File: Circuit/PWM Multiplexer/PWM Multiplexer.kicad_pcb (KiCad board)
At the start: 2 copper layers, 63 parts, among them Q1 S8050, Q10 S8050, Q11 S8050, Q12 S8050, Q13 S8050, Q14 S8050, Q2 S8050, Q3 S8050, Q4 S8050, Q5 S8050, Q6 S8050, Q7 S8050, Q8 S8050, Q9 S8050, U1 74HC137, U2 74HC137, U3 L7805

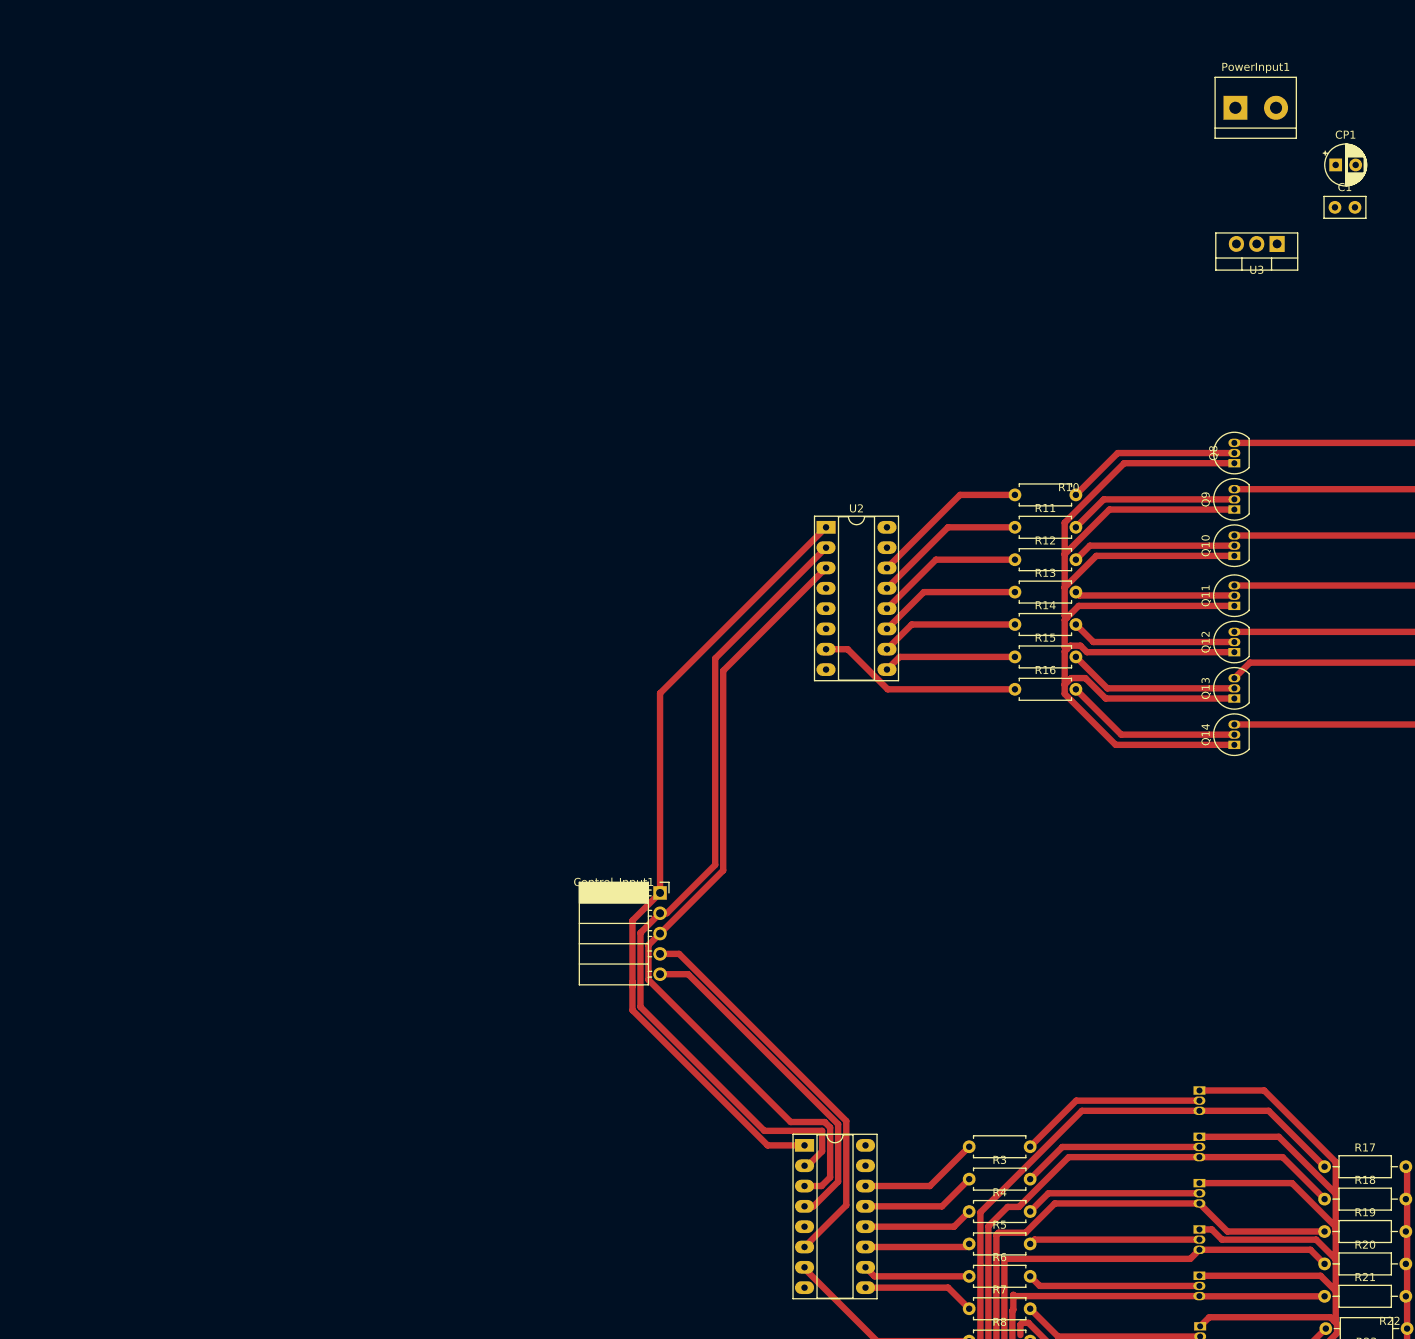
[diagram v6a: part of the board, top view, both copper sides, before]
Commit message: added optical isolation to PWM demultiplexer circuit schematic
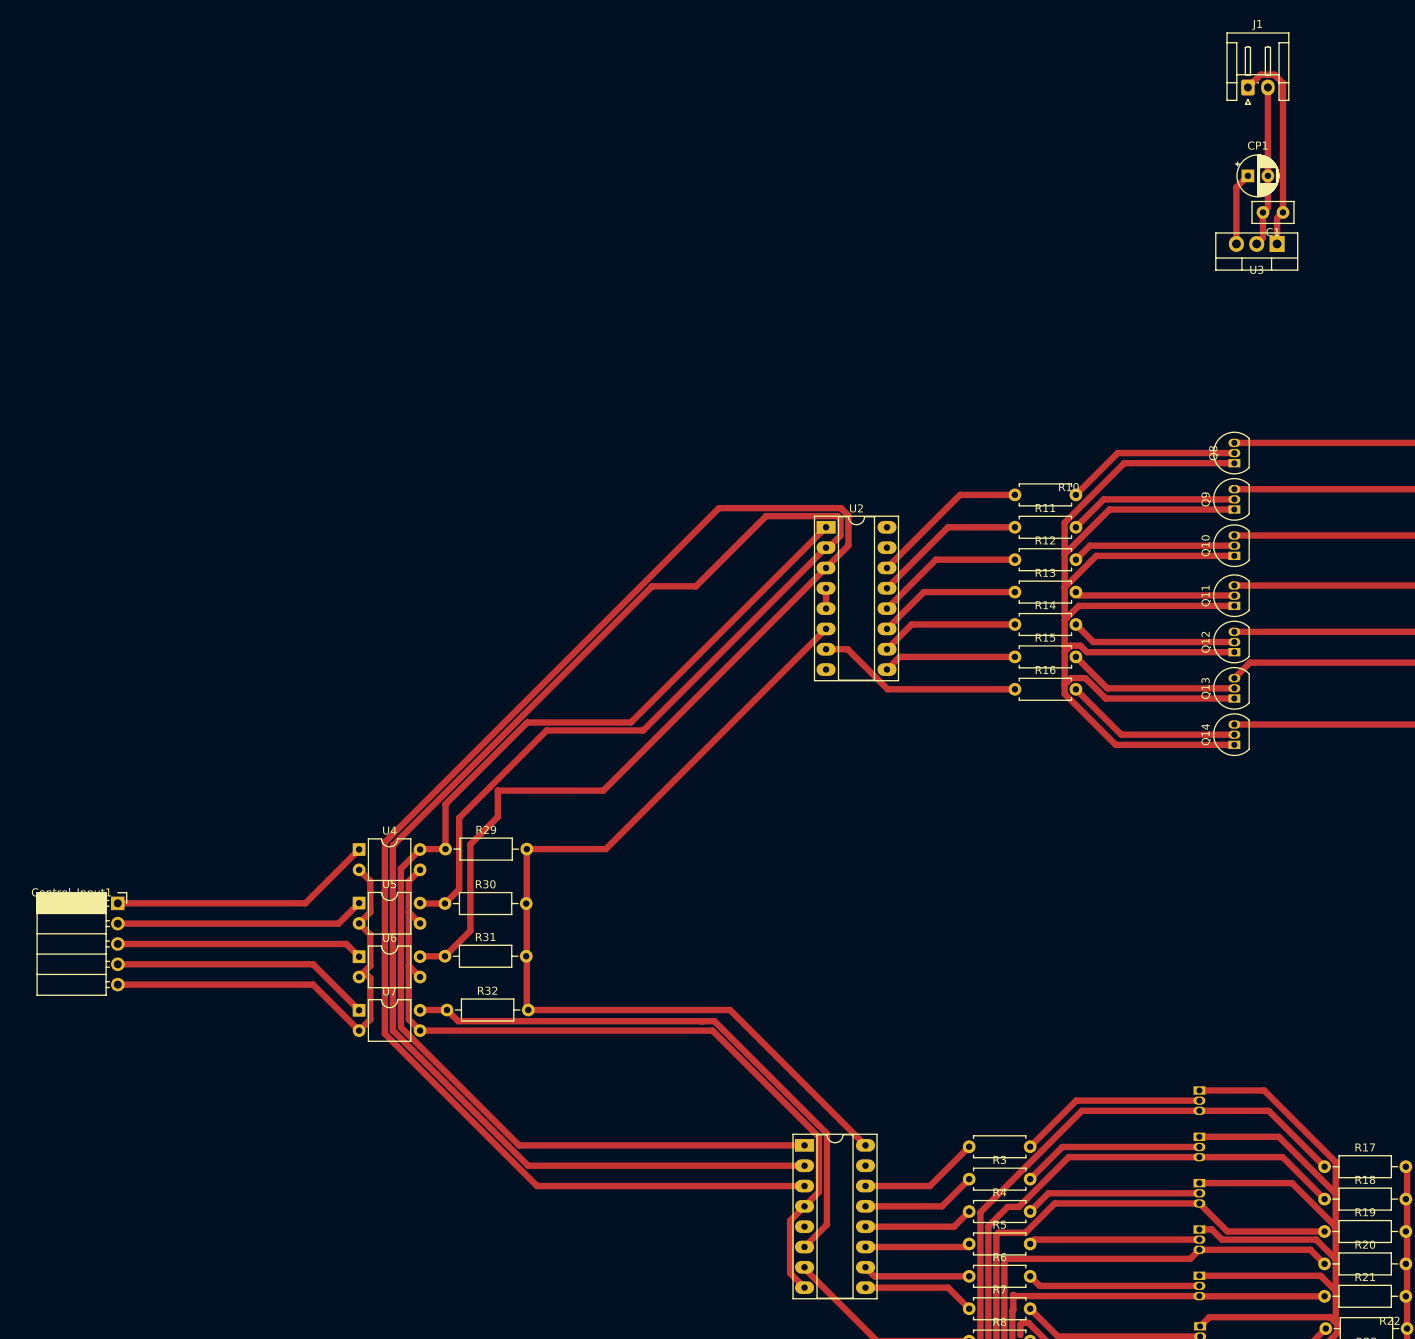
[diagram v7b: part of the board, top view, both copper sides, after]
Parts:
- removed PowerInput1: Screw_Terminal_01x02, TerminalBlock:TerminalBlock_bornier-2_P5.08mm
- added J1: JST connector, Connector_JST:JST_EH_S2B-EH_1x02_P2.50mm_Horizontal, F.Cu at (114.7, 17.8)
- added R29: 1k, Resistor_THT:R_Axial_DIN0207_L6.3mm_D2.5mm_P10.16mm_Horizontal, F.Cu at (14.4, 113.0)
- added R30: 1k, Resistor_THT:R_Axial_DIN0207_L6.3mm_D2.5mm_P10.16mm_Horizontal, F.Cu at (14.4, 119.8)
- added R31: 1k, Resistor_THT:R_Axial_DIN0207_L6.3mm_D2.5mm_P10.16mm_Horizontal, F.Cu at (14.4, 126.4)
- added R32: 1k, Resistor_THT:R_Axial_DIN0207_L6.3mm_D2.5mm_P10.16mm_Horizontal, F.Cu at (14.6, 133.1)
- added U4: PC817, Package_DIP:DIP-4_W7.62mm, F.Cu at (3.62, 113.0)
- added U5: PC817, Package_DIP:DIP-4_W7.62mm, F.Cu at (3.62, 119.7)
- added U6: PC817, Package_DIP:DIP-4_W7.62mm, F.Cu at (3.62, 126.4)
- added U7: PC817, Package_DIP:DIP-4_W7.62mm, F.Cu at (3.62, 133.1)
- moved Control_Input1 67.8 mm to (-26.5, 119.8)
- moved CP1 11.1 mm to (114.7, 28.8)
- moved C1 6.53 mm to (119.1, 33.4), turned to 180 degrees
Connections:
- Control_Input1 pad 1: A0 -> MCU_A0
- Control_Input1 pad 2: A1 -> MCU_A1
- Control_Input1 pad 3: A2 -> MCU_A2
- Control_Input1 pad 4: PWM -> MCU_PWM
- Control_Input1 pad 5: GND -> GNDA
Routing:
- net A2: track 100.9 -> 246.8 mm
- net A1: track 102.1 -> 233.7 mm
- net +5V: track 70.3 -> 197.5 mm
- net GND: track 463.8 -> 545.5 mm
- net GNDA: track 0.00 -> 56.5 mm
- net A0: track 99.4 -> 150.5 mm
- net MCU_A0: track 0.00 -> 33.0 mm
- net MCU_PWM: track 0.00 -> 32.5 mm
- net MCU_A1: track 0.00 -> 31.2 mm
- net MCU_A2: track 0.00 -> 30.8 mm
- net +12V: track 77.1 -> 102.9 mm
- net PWM: track 49.8 -> 73.1 mm
